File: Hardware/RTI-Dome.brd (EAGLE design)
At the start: 80 x 71.1 mm, 48 parts, among them IC1 24AA128ST, IC2 74LVC244, IC3 FT232RL, IC4 74ABT244, X13 PN61729-S

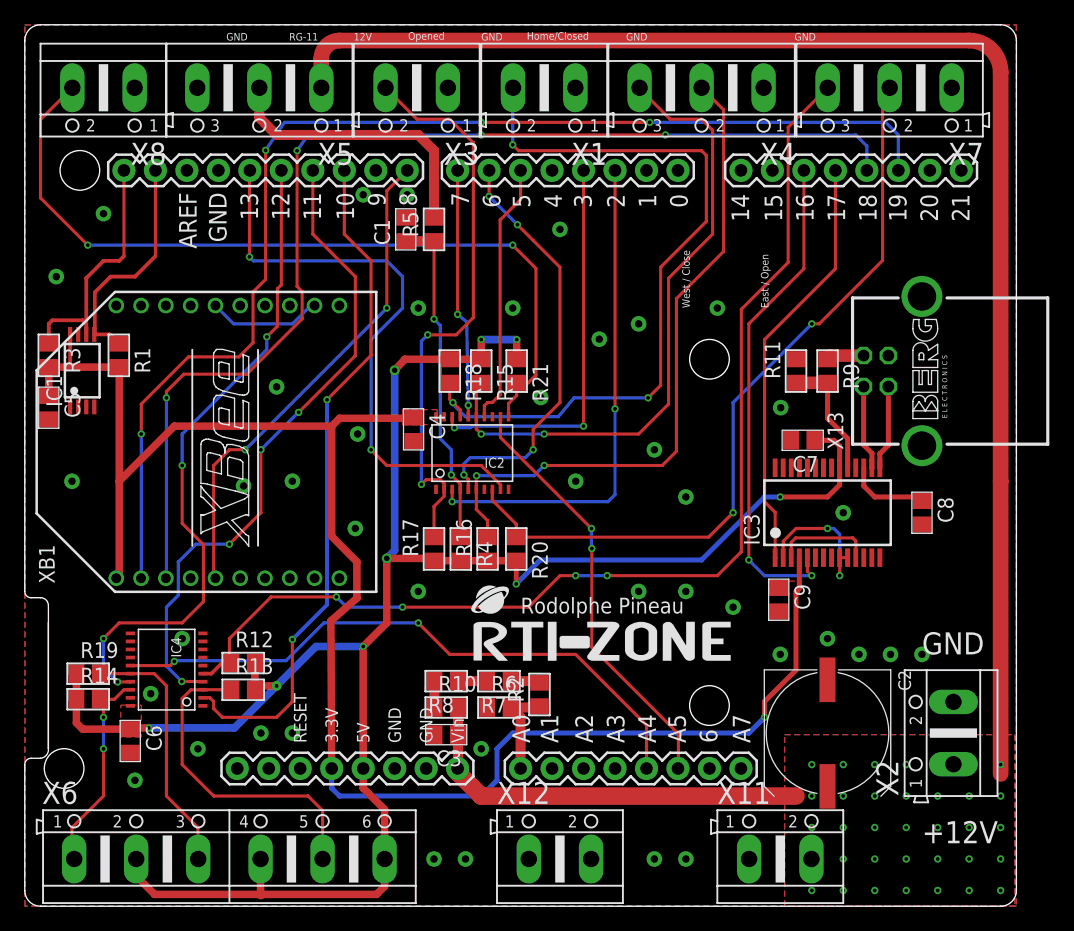
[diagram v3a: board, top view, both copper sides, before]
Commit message: Re-did the board with 74xx245 buffers instead of 244. Easier to route. Added a png to enable/disable the input buffer so that we can enable them after setting the interrupt and other things. It is disable on power up via a pull-up.
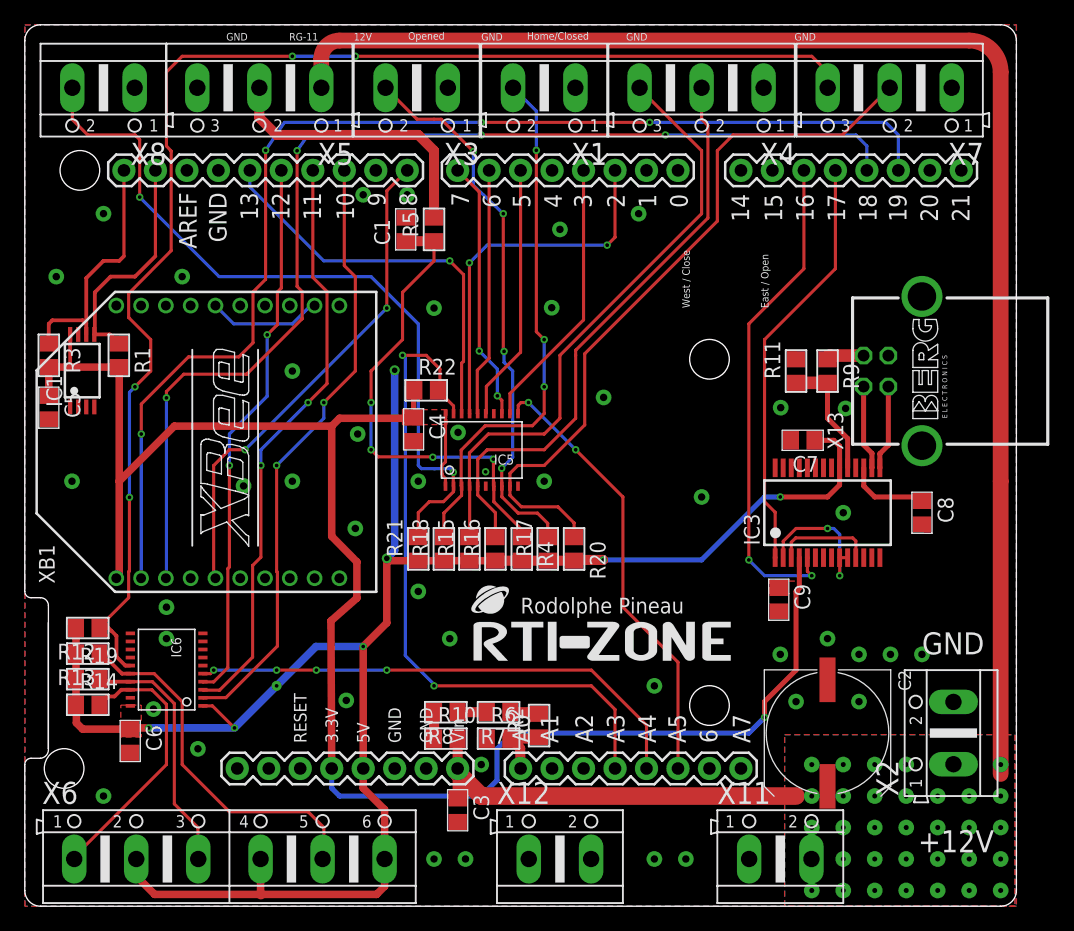
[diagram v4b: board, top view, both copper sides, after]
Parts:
- removed IC2: 74LVC244, rti:TSSOP20
- added IC5: 74LVC245, rti:TSSOP20
- added R22: 4.7K, rti:R0805
- IC6: value 74ABT244 -> 74ABT245
- moved R21 16.4 mm to (31.8, 28.8), turned to 90 degrees
- moved R15 14.4 mm to (35.9, 28.8), turned to 90 degrees
- moved R18 14.4 mm to (33.8, 28.8), turned to 90 degrees
- moved R13 12.9 mm to (5.08, 20.4), turned to 180 degrees
- moved R12 12.9 mm to (5.08, 22.4), turned to 180 degrees
- moved R17 9.18 mm to (42.2, 28.8)
- moved C3 6.17 mm to (34.9, 7.75), turned to 270 degrees
- moved R4 4.92 mm to (40.1, 28.8)
- moved R20 4.67 mm to (44.3, 28.8)
- moved R10 2.51 mm to (34.0, 13.5)
- moved R6 2.51 mm to (38.2, 13.5)
- moved R7 2.51 mm to (38.2, 15.7)
- moved R8 2.51 mm to (34.0, 15.7)
- moved R2 2.51 mm to (41.5, 14.6)
- moved R16 0.63 mm to (38.0, 28.8)
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- renumbered IC4 to IC6
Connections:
- removed net LOW_POWER: PCB1.4
- new net BUF_EN: IC5.P$19, PCB1.A3, R22.2
- new net N$4: IC5.P$14
- net 3.3V: now also IC5.P$1, IC5.P$20, R22.1; no longer IC2.P$20
- net AT_PARK_PIN: now also IC5.P$11; no longer IC2.P$12
- net AT_PARK_PIN_EXT: now also IC5.P$9; no longer IC2.P$8
- net AT_PARK_PIN_LOOP: now also IC6.P$5; no longer IC6.P$15
- net AT_PARK_PIN_LOOP_EXT: now also IC6.P$15; no longer IC6.P$5
- net BUTTON_EAST_OPEN: now also IC5.P$15; no longer IC2.P$14
- net BUTTON_EAST_OPEN_5V: now also IC5.P$5; no longer IC2.P$6
- net BUTTON_WEST_CLOSE: now also IC5.P$16; no longer IC2.P$5
- net BUTTON_WEST_CLOSE_5V: now also IC5.P$4; no longer IC2.P$15
- net D13: now also IC5.P$18; no longer IC2.P$9
- net D13_EXT: now also IC5.P$2; no longer IC2.P$11
- net GND: now also IC5.P$10, IC5.P$6, IC6.P$7, IC6.P$9; no longer IC2.P$1, IC2.P$10, IC2.P$13, IC2.P$19, IC6.P$1, IC6.P$11, IC6.P$13
- net HOME_SHUTTER_CLOSED: now also IC5.P$17; no longer IC2.P$3
- net HOME_SHUTTER_CLOSED_5V: now also IC5.P$3; no longer IC2.P$17
- net M_DIR: now also IC6.P$3; no longer IC6.P$4
- net M_DIR_5V: now also IC6.P$17; no longer IC6.P$16
- net M_STEP: now also IC6.P$4; no longer IC6.P$17
- net M_STEP_5V: now also IC6.P$16; no longer IC6.P$3
- net RG-11: now also IC5.P$13; no longer IC2.P$16
- net RG-11-IN_5V: now also IC5.P$7; no longer IC2.P$4
- net SHUTTER_OPENED: now also IC5.P$12; no longer IC2.P$18
- net SHUTTER_OPENED_5V: now also IC5.P$8; no longer IC2.P$2
- net VCC: now also IC6.P$1
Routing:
- net BUF_EN: track 0.00 -> 55.5 mm, vias 0 -> 2
- net HOME_SHUTTER_CLOSED_5V: track 62.2 -> 42.9 mm
- net AT_PARK_PIN_LOOP_EXT: track 89.9 -> 109.1 mm
- net D13: track 47.0 -> 32.8 mm, vias 2 -> 1
- net BUTTON_WEST_CLOSE: track 34.1 -> 20.0 mm, vias 4 -> 0
- net VCC: track 163.4 -> 150.6 mm, vias 9 -> 8
- net RG-11-IN_5V: track 27.1 -> 38.6 mm, vias 2 -> 4
- net HOME_SHUTTER_CLOSED: track 40.5 -> 30.2 mm
- net SHUTTER_OPENED: track 32.1 -> 22.1 mm, vias 2 -> 0
- net AT_PARK_PIN_LOOP: track 50.0 -> 41.3 mm, vias 2 -> 4
- net M_STEP: track 53.1 -> 44.4 mm, vias 4 -> 2
- net 3.3V: track 138.1 -> 146.4 mm
- net BUTTON_EAST_OPEN_5V: track 53.9 -> 47.5 mm, vias 2 -> 0
- net M_EN: track 55.1 -> 49.2 mm
- net M_DIR: track 52.8 -> 47.4 mm, vias 4 -> 2
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
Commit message: Fix legend on PCB.
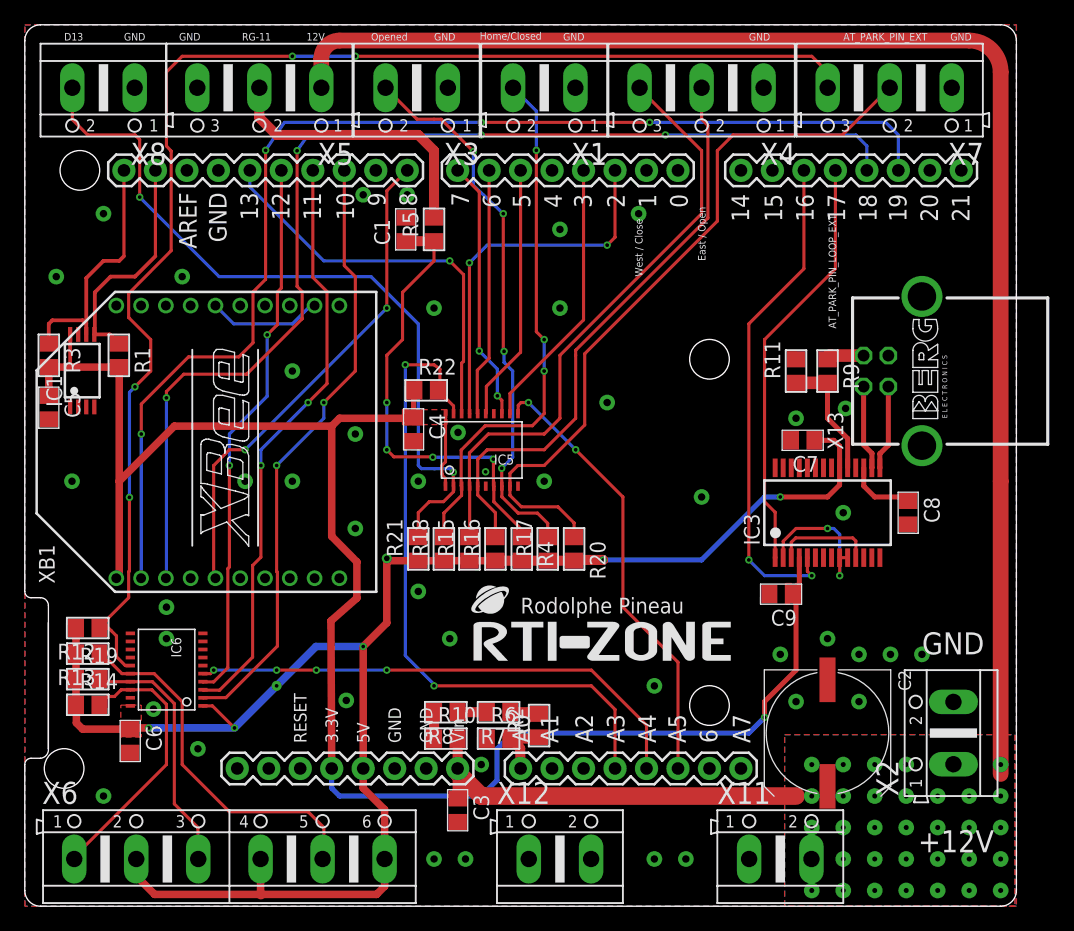
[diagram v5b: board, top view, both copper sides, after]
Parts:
- moved C8 1.11 mm to (71.3, 31.8)
- moved C9 0.48 mm to (61.0, 25.2), turned to 180 degrees
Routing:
- net VCC: track 150.6 -> 135.2 mm, vias 8 -> 7
- net RG-11-IN_5V: track 38.6 -> 36.8 mm
- net BUF_EN: track 55.5 -> 54.1 mm
- net N$6: track 6.75 -> 5.56 mm
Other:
- board text added: "AT_PARK_PIN_EXT"
- board text added: "AT_PARK_PIN_LOOP_EXT"
- board text added: "D13"

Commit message: Better homing code. Does necessarily stop at home bug sinf home via an interrupt. I'll add more got to go back home after passing it. It does however return the proper position after homing. Added more board for ENC424J600 ethernet chip. Fix position of the headers.
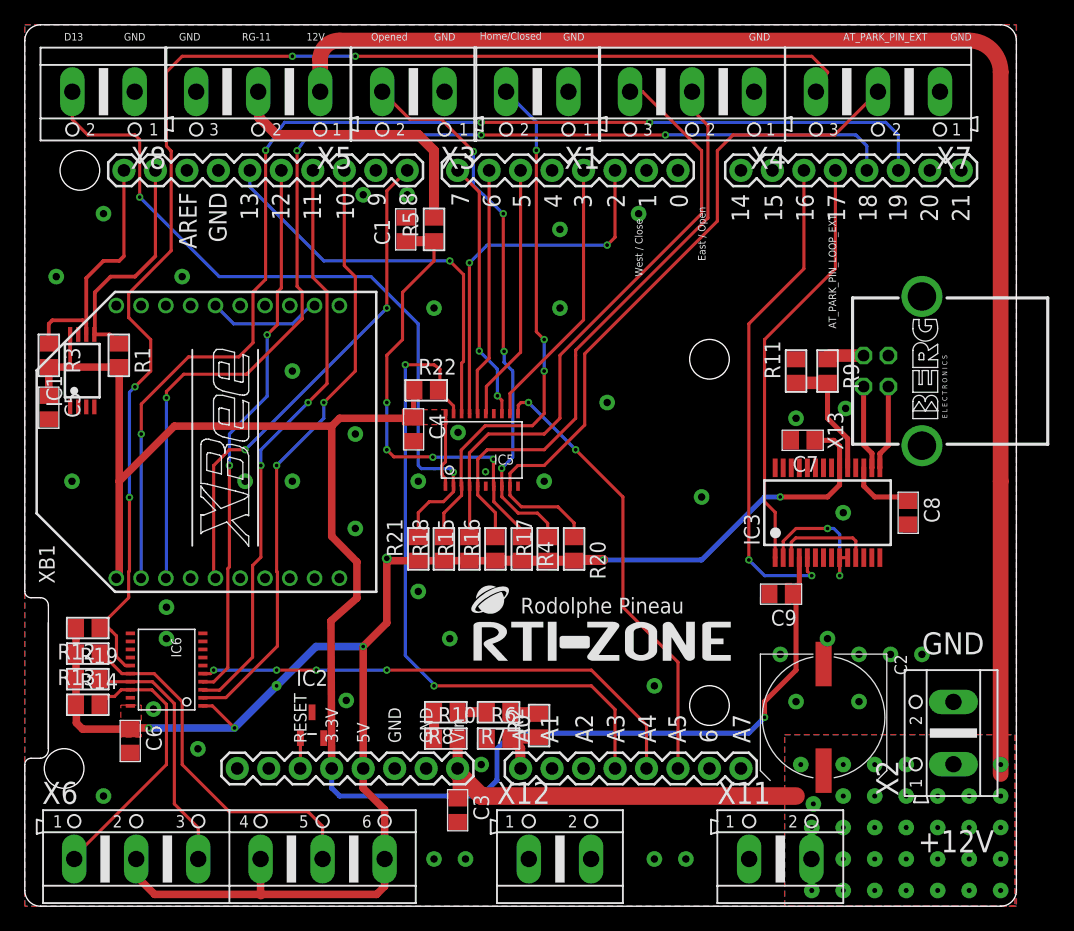
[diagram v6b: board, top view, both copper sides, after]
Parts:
- added IC2: MCP120T-270I_TT, MCP120T-270I_TT:SOT95P237X112-3N
- moved C2 1.31 mm to (64.5, 15.2)
- moved X7 1.00 mm to (68.8, 65.7)
- moved X4 0.83 mm to (53.8, 65.7)
- moved X1 0.64 mm to (41.4, 65.7)
- moved X3 0.42 mm to (31.4, 65.7)
- moved X5 0.33 mm to (18.8, 65.7)
- moved X8 0.32 mm to (6.35, 65.7)
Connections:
- new net RESET: IC2.1, PCB1.RESET
- net 3.3V: now also IC2.2
- net GND: now also IC2.3
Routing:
- net RESET: track 0.00 -> 2.46 mm
- net AT_PARK_PIN_EXT: track 59.3 -> 58.2 mm
- net 3.3V: track 146.4 -> 147.1 mm
- net BUTTON_WEST_CLOSE_5V: track 48.7 -> 49.3 mm
- net AT_PARK_PIN_LOOP_EXT: track 109.1 -> 109.7 mm

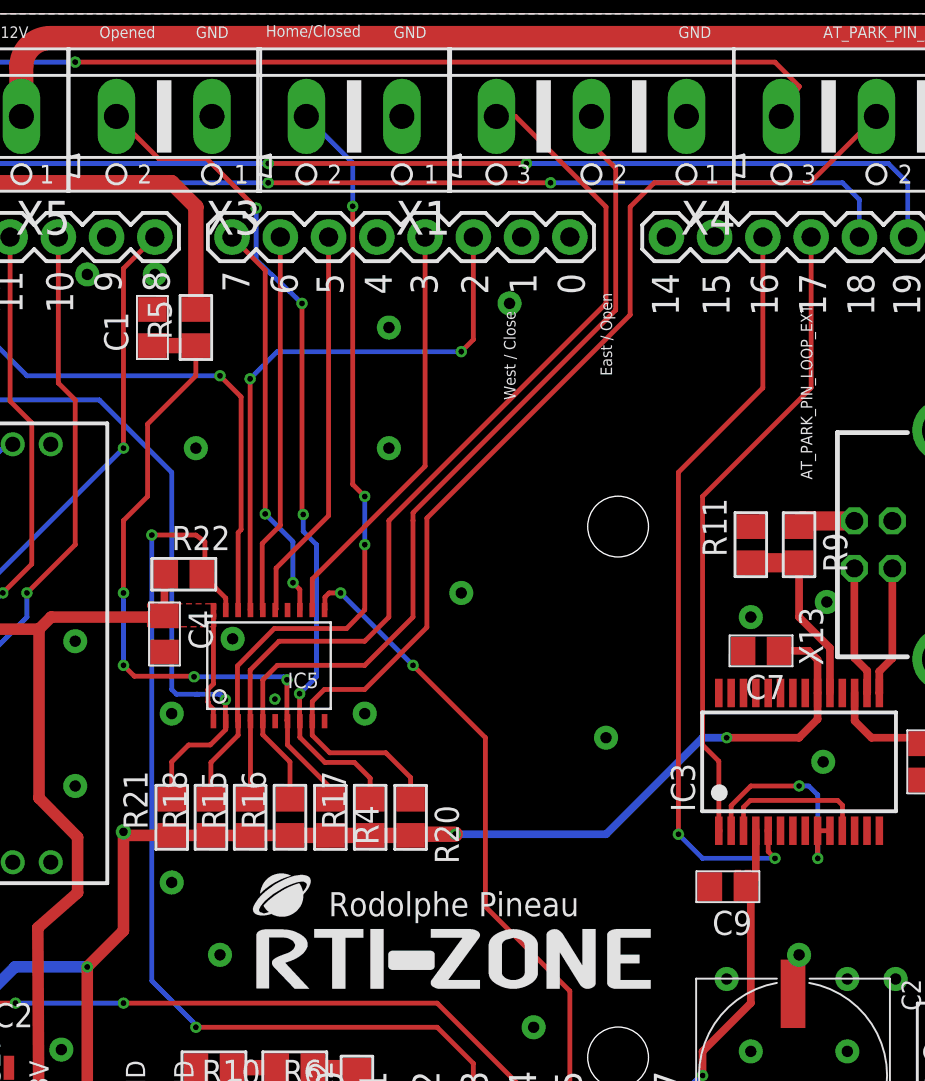
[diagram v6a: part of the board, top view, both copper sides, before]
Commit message: Fix all board for proper header alignement. New code for homing (and calibrating) tested and works.
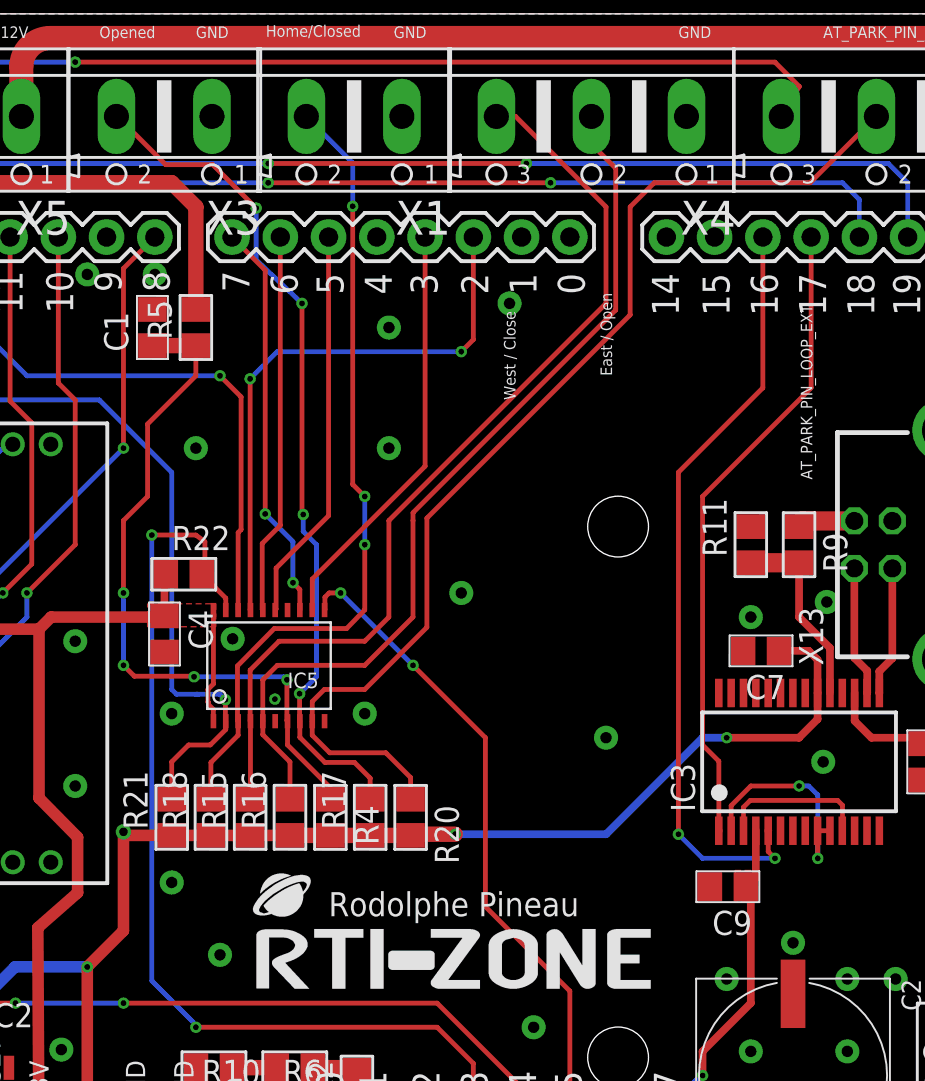
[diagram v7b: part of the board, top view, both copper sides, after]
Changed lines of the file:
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@@
 <via x="34.29" y="21.59" extent="1-16" drill="0.6" diameter="1.27"/>
 <via x="54.61" y="33.02" extent="1-16" drill="0.6" diameter="1.27"/>
-<via x="64.77" y="21.59" extent="1-16" drill="0.6" diameter="1.27"/>
+<via x="64.4525" y="22.225" extent="1-16" drill="0.6" diameter="1.27"/>
 <via x="67.31" y="20.32" extent="1-16" drill="0.6" diameter="1.27"/>
 <via x="69.85" y="20.32" extent="1-16" drill="0.6" diameter="1.27"/>
@@
 <wire x1="41.37025" y1="31.71825" x2="42.19575" y2="30.89275" width="0.254" layer="1"/>
 <wire x1="42.19575" y1="30.89275" x2="42.19575" y2="29.779" width="0.254" layer="1"/>
-<wire x1="33.5915" y1="63.5" x2="36.195" y2="60.8965" width="0.254" layer="1"/>
 <via x="36.195" y="60.8965" extent="1-16" drill="0.3" diameter="0.254"/>
 <wire x1="36.195" y1="60.8965" x2="36.195" y2="58.166" width="0.254" layer="16"/>
@@
 <wire x1="39.37" y1="43.18" x2="39.37" y2="36.22675" width="0.254" layer="16"/>
 <wire x1="39.37" y1="36.22675" x2="38.481" y2="35.33775" width="0.254" layer="16"/>
-<wire x1="28.8384" y1="65.7225" x2="31.0609" y2="63.5" width="0.254" layer="1"/>
-<wire x1="31.0609" y1="63.5" x2="33.5915" y2="63.5" width="0.254" layer="1"/>
+<wire x1="36.195" y1="60.8965" x2="33.909" y2="63.1825" width="0.254" layer="1"/>
+<wire x1="33.909" y1="63.1825" x2="31.4325" y2="63.1825" width="0.254" layer="1"/>
+<wire x1="31.4325" y1="63.1825" x2="28.8925" y2="65.7225" width="0.254" layer="1"/>
+<wire x1="28.8925" y1="65.7225" x2="28.8384" y2="65.7225" width="0.254" layer="1"/>
 </signal>
 <signal name="HOME_SHUTTER_CLOSED_5V">
